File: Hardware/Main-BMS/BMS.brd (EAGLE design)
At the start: 114.3 x 124.5 mm, 99 parts, among them IC1 ACS759, IC2 SMI-1324-TW-5V-2-R, Q1 2N7002PW, Q10 2N7002PW, Q2 2N7002PW, Q5 2N7002PW, Q6 2N7002PW, Q7 2N7002PW, Q8 2N7002PW, Q9 2N7002PW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

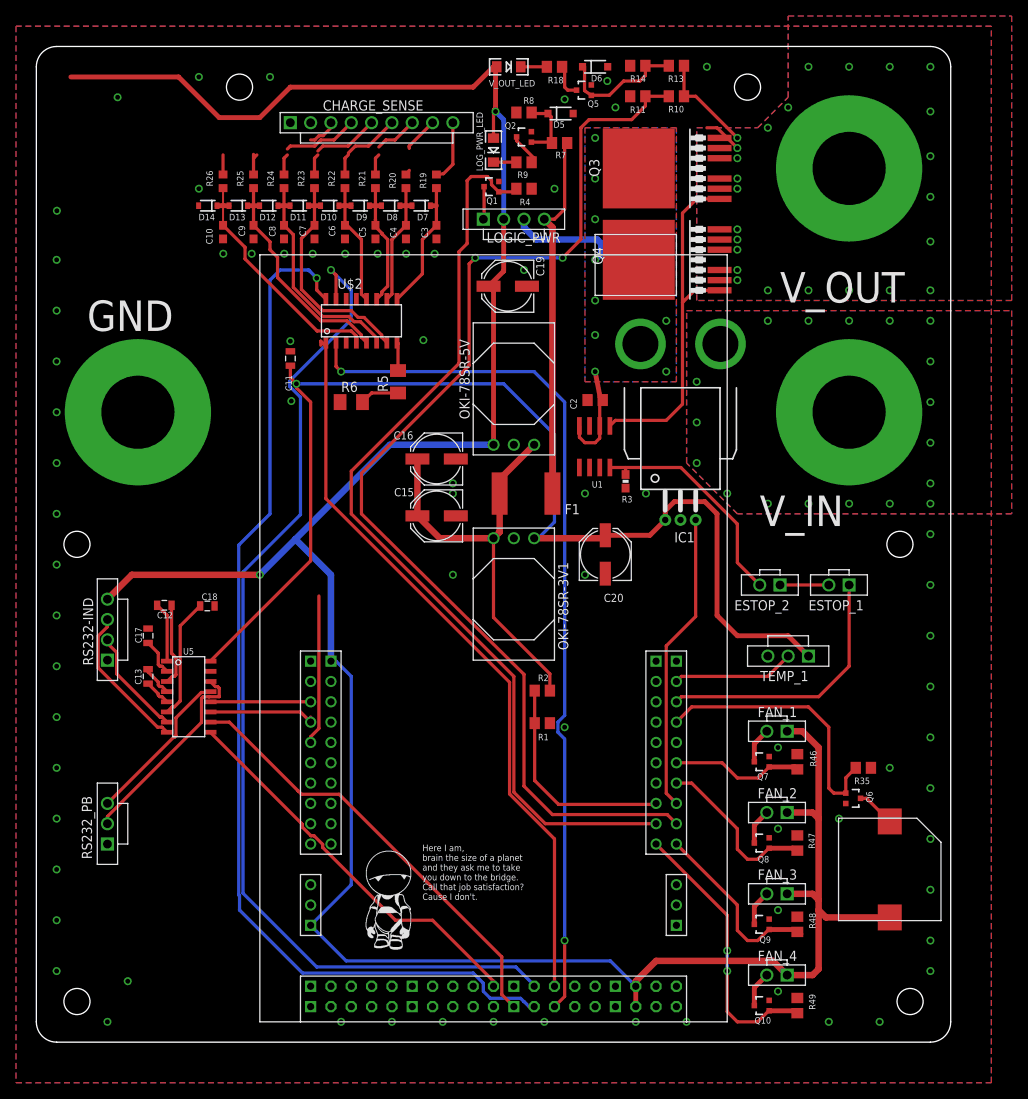
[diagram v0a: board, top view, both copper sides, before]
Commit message: Fixed connector placement, switched to 3v3 UART for indicator board and added protection zeners, replaced ACS759 with ACS770.
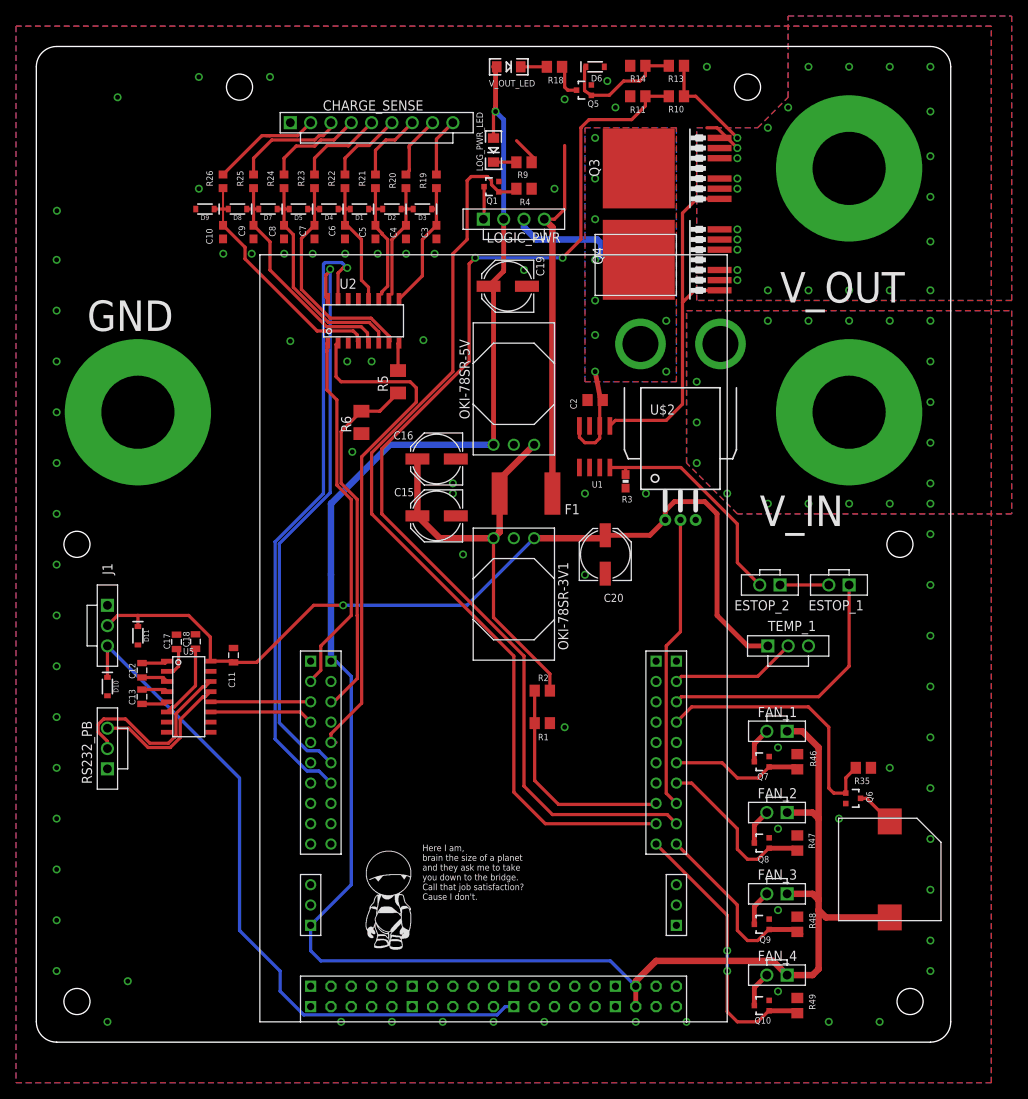
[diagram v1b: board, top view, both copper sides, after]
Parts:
- removed D12, D13, D14: PDZ7.5B, SparkFun-DiscreteSemi:SOD-323
- removed IC1: ACS759, MRDT-ICs:ACS-PFF-LEADFORM
- removed Q2: 2N7002PW, SparkFun-DiscreteSemi:SOT323
- removed R7: 1MΩ, rcl:R0805
- removed R8: 100kΩ, rcl:R0805
- removed RS232-IND: SL04VERT, MRDT-Connectors:MOLEX-70543-0003
- added D1, D2, D3, D4: 7.5V, SparkFun-DiscreteSemi:SOD-323
- added J1: SL03, MRDT-Connectors:MOLEX-70543-0002
- added U2: MUX508, MRDT-ICs:SOIC16
- D10, D11: value PDZ7.5B -> 3.6V
- D5: value BZT52C15-7-F -> 7.5V; device SparkFun-DiscreteSemi:SOD-123 -> SparkFun-DiscreteSemi:SOD-323
- D6: value BZT52C15-7-F -> 3.6V; device SparkFun-DiscreteSemi:SOD-123 -> SparkFun-DiscreteSemi:SOD-323
- D7, D8, D9: value PDZ7.5B -> 7.5V
- U$2: value MUX508 -> ACS770; device MRDT-ICs:SOIC16 -> MRDT-ICs:ACS-PFF-LEADFORM
- moved D10 66.2 mm to (8.89, 44.5), turned to 270 degrees
- moved D11 57.4 mm to (12.7, 50.8), turned to 270 degrees
- moved U$2 47.0 mm to (80.5, 65.3)
- moved C11 37.8 mm to (24.6, 48.4)
- moved D5 34.9 mm to (32.8, 104.1), turned to 180 degrees
- moved D9 19.4 mm to (21.1, 104.1)
- moved D7 19.2 mm to (29.0, 104.1)
- moved D8 19.2 mm to (25.1, 104.1)
- moved RS232_PB 9.40 mm to (8.89, 36.7)
- moved C12 8.59 mm to (13.2, 46.5), turned to 270 degrees
- moved C18 4.69 mm to (19.9, 50.1), turned to 90 degrees
- moved C17 3.64 mm to (17.5, 50.0)
- moved R6 2.84 mm to (40.6, 77.5), turned to 90 degrees
- moved C13 2.65 mm to (13.2, 43.2)
- moved TEMP_1 1.27 mm to (94.0, 49.5), turned to 180 degrees
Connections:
- removed net GAUGE_ON: U3.9.0
- removed net LED_CLR: U3.9.1
- removed net LED_SRCK: U3.8.7
- removed net N$13: D5.C, Q2.1, R7.2, R8.1
- removed net N$23: U$2.13
- removed net N$5: IC1.P$2, V_IN.P$1
- removed net RS232_RX_IND: RS232-IND.3, U5.8
- removed net RS232_TX_IND: RS232-IND.2, U5.7
- net +3V3: now also D11.C, J1.2, U$2.1; no longer IC1.1
- net 5V: no longer RS232-IND.4
- net ADC_CELL_A0: now also U2.1, U3.6.0; no longer U$2.1, U3.7.6
- net ADC_CELL_A1: now also U2.16, U3.4.4; no longer U$2.16, U3.7.5
- net ADC_CELL_A2: now also U2.15, U3.4.5; no longer U$2.15, U3.7.4
- net ADC_CELL_EN: now also U2.2, U3.4.2; no longer U$2.2, U3.7.7
- net ADC_CELL_VOUT: now also U3.6.1; no longer U3.4.1
- net CELL_1_FILTER: now also D8.A, D9.C, U2.4; no longer D13.A, D14.C, U$2.4
- net CELL_2_FILTER: now also D7.A, D8.C, U2.5; no longer D12.A, D13.C, U$2.5
- net CELL_3_FILTER: now also D5.A, D7.C, U2.6; no longer D11.A, D12.C, U$2.6
- net CELL_4_FILTER: now also D4.A, D5.C, U2.7; no longer D10.A, D11.C, U$2.7
- net CELL_5_FILTER: now also D1.A, D4.C, U2.12; no longer D10.C, D9.A, U$2.12
- net CELL_6_FILTER: now also D1.C, D2.A, U2.11; no longer D8.A, D9.C, U$2.11
- net CELL_7_FILTER: now also D2.C, D3.A, U2.10; no longer D7.A, D8.C, U$2.10
- net CELL_8_FILTER: now also D3.C, U2.9; no longer D7.C, U$2.9
- net GND: now also D10.A, D11.A, D9.A, J1.1, R9.2, U2.3; no longer D14.A, D5.A, IC1.2, Q2.2, R8.2, RS232-IND.1, U$2.14
- net N$11: now also U$2.P$2, V_IN.P$1; no longer Q2.3, R9.2
- net N$15: no longer R7.1
- net N$22: now also U2.8; no longer U$2.8
- net N$41: now also U$2.P$1; no longer IC1.P$1
- net PACK_I_MEAS: now also U$2.2; no longer IC1.3
- net SER_RX_IND: no longer U5.9
- net SER_TX_IND: now also D10.C, J1.3; no longer U5.10
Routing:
- net 5V: track 342.7 -> 258.0 mm, vias 2 -> 1
- net ADC_CELL_A1: track 132.9 -> 72.0 mm
- net ADC_CELL_A2: track 130.9 -> 79.1 mm
- net SER_RX_IND: track 49.4 -> 0.00 mm
- net ADC_CELL_A0: track 92.3 -> 45.9 mm
- net ADC_CELL_EN: track 110.2 -> 64.4 mm, vias 2 -> 0
- net +3V3: track 144.7 -> 112.6 mm
- net SER_TX_IND: track 55.5 -> 86.9 mm
- net ADC_CELL_VOUT: track 23.7 -> 45.3 mm
- net RS232_RX_IND: track 18.5 -> 0.00 mm
- net RS232_TX_IND: track 13.5 -> 0.00 mm
- net CELL_1: track 2.45 -> 14.1 mm
- net N$13: track 8.45 -> 0.00 mm
- net N$42: track 10.4 -> 3.35 mm
- net CELL_2: track 6.28 -> 13.3 mm
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- added copper zone on layer 1, net N$11
- removed copper zone on layer 1, net N$5

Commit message: Updated to actually match last commit
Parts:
- moved D10 15.0 mm to (9.14, 59.4), turned to 90 degrees
- turned J1 to 270 degrees
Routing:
- net SER_TX_IND: track 86.9 -> 91.8 mm
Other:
- board text added: "SER_IND"
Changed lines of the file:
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@@
 Call that job satisfaction?
 Cause I don't.</text>
+<text x="6.35" y="48.26" size="1.27" layer="21" rot="R90">SER_IND</text>
 </plain>
 <attributes>
@@
 <element name="R5" library="rcl" package="M1206" value="1M" x="45.212" y="82.55" rot="R90"/>
 <element name="R6" library="rcl" package="M1206" value="100k" x="40.64" y="77.47" rot="R90"/>
-<element name="J1" library="MRDT-Connectors" package="MOLEX-70543-0002" value="SL03" x="8.89" y="52.07" rot="R90"/>
+<element name="J1" library="MRDT-Connectors" package="MOLEX-70543-0002" value="SL03" x="8.89" y="52.07" rot="R270"/>
 <element name="U2" library="MRDT-ICs" package="SOIC16" value="MUX508" x="40.894" y="90.17"/>
 <element name="D1" library="SparkFun-DiscreteSemi" package="SOD-323" value="7.5V" x="40.386" y="104.14" rot="R180">
@@
 </element>
 <element name="U$2" library="MRDT-ICs" package="ACS-PFF-LEADFORM" value="ACS770" x="80.518" y="65.278"/>
-<element name="D10" library="SparkFun-DiscreteSemi" package="SOD-323" value="3.6V" x="8.89" y="44.45" rot="R270">
-<attribute name="PROD_ID" value="DIO-08199" x="8.89" y="44.45" size="1.778" layer="27" rot="R270" display="off"/>
+<element name="D10" library="SparkFun-DiscreteSemi" package="SOD-323" value="3.6V" x="9.144" y="59.436" rot="R90">
+<attribute name="PROD_ID" value="DIO-08199" x="9.144" y="59.436" size="1.778" layer="27" rot="R90" display="off"/>
 </element>
 <element name="D11" library="SparkFun-DiscreteSemi" package="SOD-323" value="3.6V" x="12.7" y="50.8" rot="R270">
@@
 <wire x1="24.6488" y1="47.4698" x2="27.53545625" y2="47.4698" width="0.4064" layer="1"/>
 <contactref element="J1" pad="2"/>
-<wire x1="10.16" y1="53.34" x2="8.89" y2="52.07" width="0.4064" layer="1"/>
-<wire x1="12.7" y1="53.34" x2="10.16" y2="53.34" width="0.4064" layer="1"/>
-<wire x1="12.7" y1="53.34" x2="19.05" y2="53.34" width="0.4064" layer="1"/>
+<wire x1="19.05" y1="53.34" x2="12.7" y2="53.34" width="0.4064" layer="1"/>
 <wire x1="19.05" y1="53.34" x2="21.75" y2="50.64" width="0.4064" layer="1"/>
 <wire x1="21.75" y1="50.64" x2="21.75" y2="47.625" width="0.4064" layer="1"/>
@@
 <wire x1="78.618" y1="65.278" x2="76.7" y2="63.36" width="0.6096" layer="1"/>
 <wire x1="12.7" y1="51.95" x2="12.7" y2="53.34" width="0.4064" layer="1"/>
+<wire x1="12.7" y1="53.34" x2="10.16" y2="53.34" width="0.4064" layer="1"/>
+<wire x1="10.16" y1="53.34" x2="8.89" y2="52.07" width="0.4064" layer="1"/>
 </signal>
 <signal name="N$3">
@@
 <contactref element="U3" pad="9.7"/>
 <contactref element="J1" pad="3"/>
-<wire x1="8.89" y1="49.53" x2="25.4" y2="33.02" width="0.4064" layer="16"/>
-<wire x1="25.4" y1="33.02" x2="25.4" y2="13.97" width="0.4064" layer="16"/>
 <wire x1="25.4" y1="13.97" x2="30.48" y2="8.89" width="0.4064" layer="16"/>
 <wire x1="30.48" y1="8.89" x2="30.48" y2="6.35" width="0.4064" layer="16"/>
@@
 <wire x1="33.4192" y1="3.4108" x2="57.57838125" y2="3.4108" width="0.4064" layer="16"/>
 <contactref element="D10" pad="C"/>
-<wire x1="8.89" y1="45.6" x2="8.89" y2="49.53" width="0.4064" layer="1"/>
+<wire x1="8.89" y1="54.61" x2="25.4" y2="38.1" width="0.4064" layer="16"/>
+<wire x1="25.4" y1="38.1" x2="25.4" y2="13.97" width="0.4064" layer="16"/>
+<wire x1="9.144" y1="58.286" x2="8.89" y2="58.032" width="0.4064" layer="1"/>
+<wire x1="8.89" y1="58.032" x2="8.89" y2="54.61" width="0.4064" layer="1"/>
 </signal>
 <signal name="SER_RX_PB">

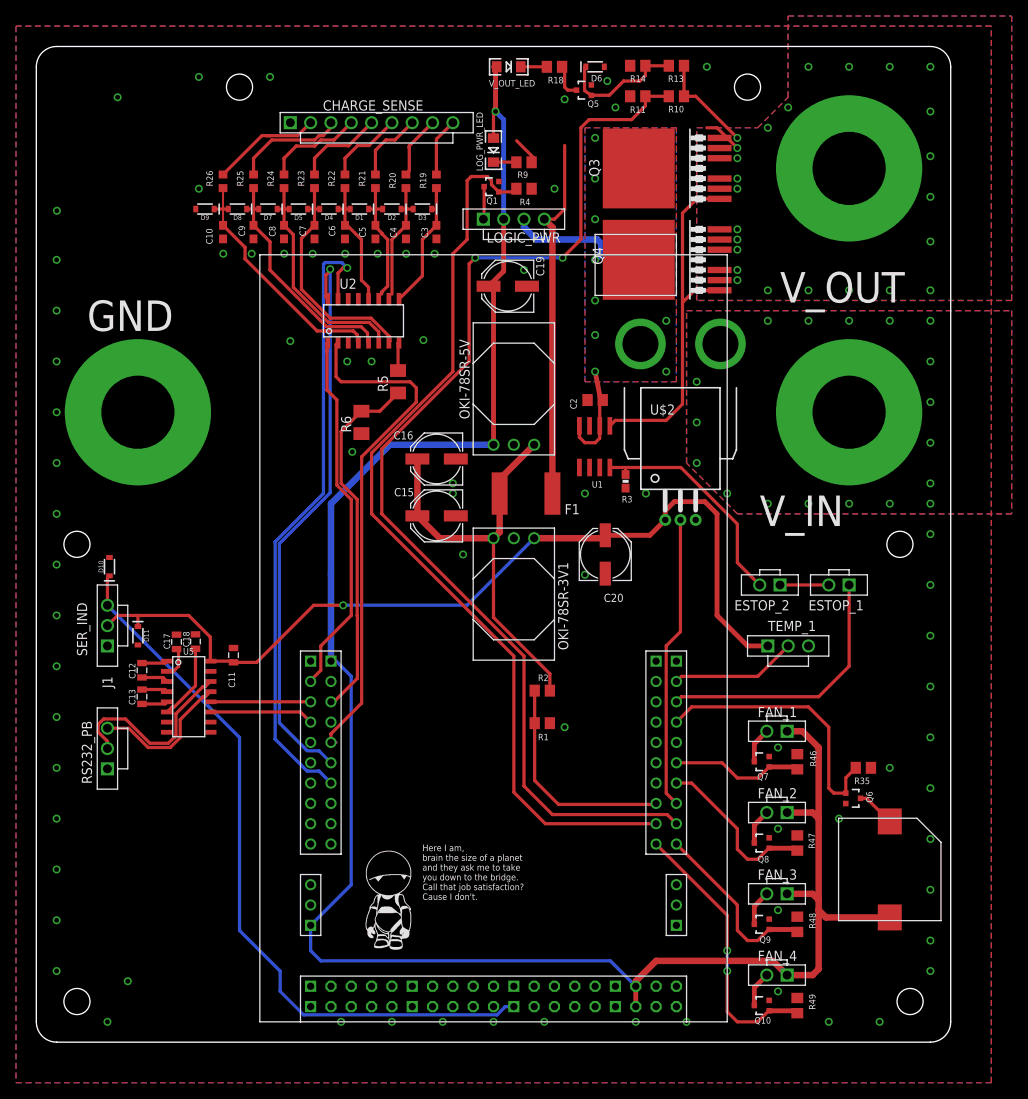
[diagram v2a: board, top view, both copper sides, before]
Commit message: Cleaned Routing and Silkscreen
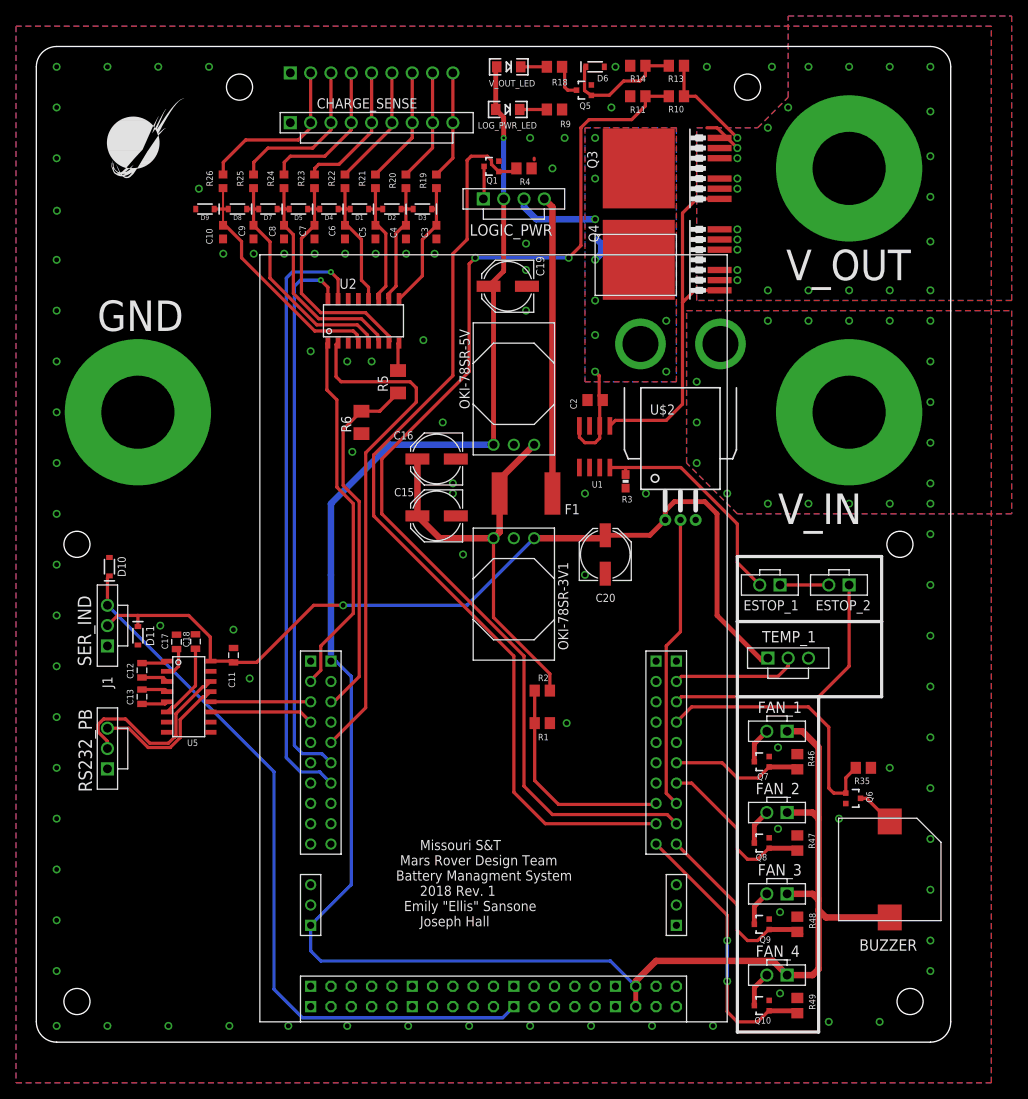
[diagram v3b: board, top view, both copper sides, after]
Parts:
- removed U$1: (no value), sig:MARVIN-THE-PARANOID-ANDROID
- removed U$17: (no value), sig:SANSONE-SIG
- added CHARGE_SENSE1: SL09, MRDT-Connectors:MOLEX-70543-0008
- moved U$9 19.3 mm to (8.81, 107.2), flipped to the top
- moved R9 7.62 mm to (64.8, 116.6)
- moved LOG_PWR_LED 5.38 mm to (58.9, 116.6), turned to 0 degrees
- moved Q1 2.54 mm to (56.9, 109.5)
- moved LOGIC_PWR 2.54 mm to (59.7, 105.4)
- moved R4 2.54 mm to (61.0, 109.2)
- moved TEMP_1 1.52 mm to (94.0, 48.0)
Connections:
- net CELL_1: now also CHARGE_SENSE1.2
- net CELL_2: now also CHARGE_SENSE1.3
- net CELL_3: now also CHARGE_SENSE1.4
- net CELL_4: now also CHARGE_SENSE1.5
- net CELL_5: now also CHARGE_SENSE1.6
- net CELL_6: now also CHARGE_SENSE1.7
- net CELL_7: now also CHARGE_SENSE1.8
- net CELL_8: now also CHARGE_SENSE1.9
- net GND: now also CHARGE_SENSE1.1
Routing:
- net N$15: track 45.7 -> 37.3 mm
- net CELL_2: track 13.3 -> 20.6 mm
- net CELL_1: track 14.1 -> 21.1 mm
- net CELL_3: track 12.3 -> 18.7 mm
- net CELL_8: track 7.33 -> 13.6 mm
- net CELL_4: track 11.1 -> 17.1 mm
- net CELL_7: track 8.10 -> 14.1 mm
- net CELL_6: track 9.05 -> 14.6 mm
- net CELL_5: track 9.74 -> 15.1 mm
- net 5V: track 258.0 -> 253.7 mm
- net GND: track 3.74 -> 0.19 mm, vias 73 -> 87
- net ADC_CELL_A1: track 72.0 -> 69.2 mm
- net ADC_CELL_A2: track 79.1 -> 76.5 mm
- net LOGIC_SWITCH: track 115.8 -> 118.1 mm
- net CELL_7_FILTER: track 15.4 -> 16.6 mm
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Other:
- board text added: "BUZZER"
- board text added: "Missouri S&T Mars Rover Design Team Battery Managment System 2018 Rev. 1 Emily "Ellis" Sansone Joseph Hall"
- board text removed: "Here I am, brain the size of a planet and they ask me to take you down to the bridge. Call that job satisfaction? Cause I don't."
- board text removed: "Missouri S&T Mars Rover Design Team Battery Management System Rev. 2, Gryphon Emily "Ellis" Sansone"

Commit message: Cleaned up fonts, connectors, MUX508 traces and symbol. Removed some via stitching to reduce short potential with drill-hole washers.
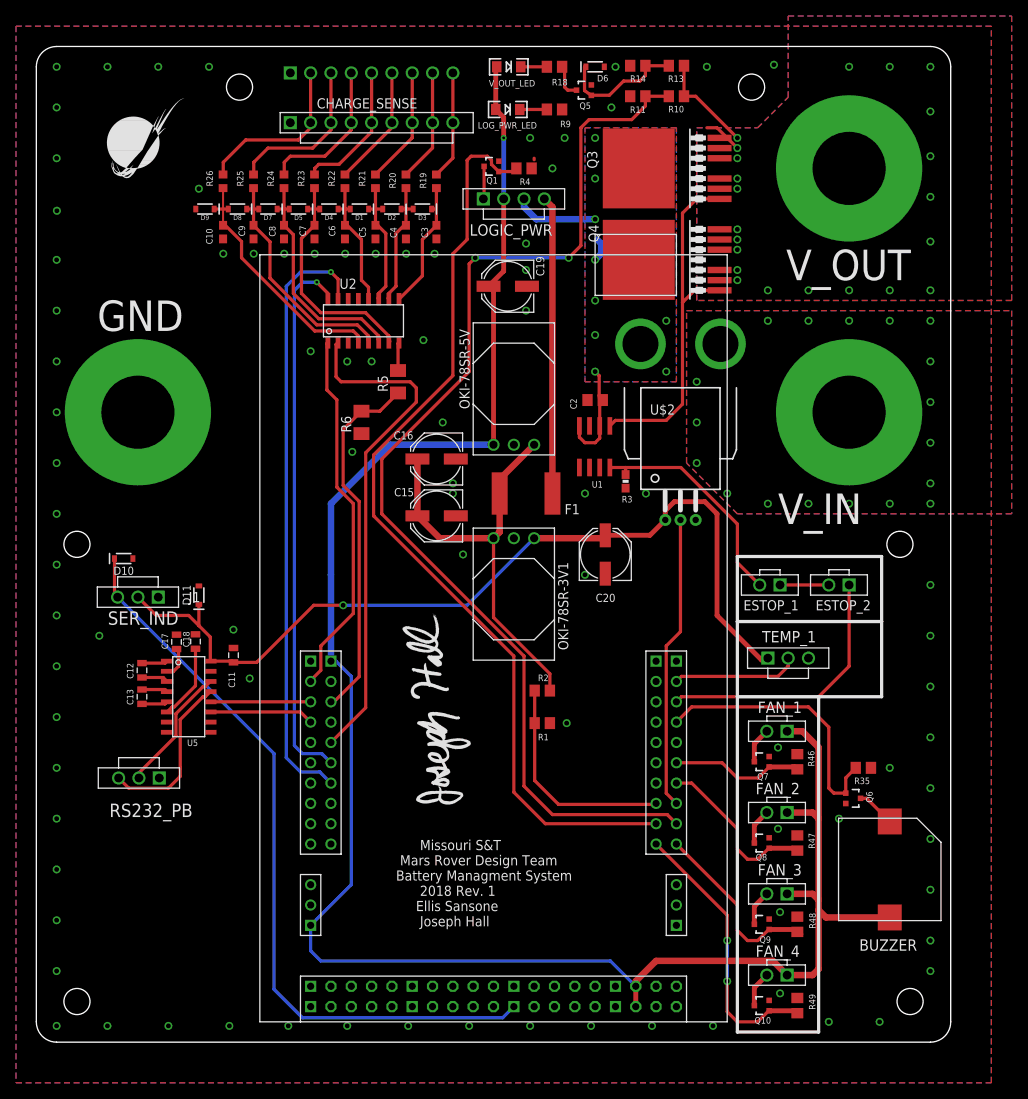
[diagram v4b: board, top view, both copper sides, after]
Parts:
- added U$1: (no value), MRDT-Signatures:JOSEPH_HALL_SIGNATURE
- moved D11 9.16 mm to (20.3, 55.9), turned to 90 degrees
- moved RS232_PB 5.39 mm to (12.8, 33.0), turned to 0 degrees
- moved J1 5.21 mm to (12.7, 55.6), turned to 0 degrees
- moved D10 2.05 mm to (10.9, 60.5), turned to 0 degrees
- moved H4 0.51 mm to (89.4, 119.4)
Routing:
- net RS232_TX_PB: track 23.9 -> 15.9 mm
- net RS232_RX_PB: track 18.1 -> 21.2 mm
- net +3V3: track 113.4 -> 111.3 mm
- net SER_TX_IND: track 92.4 -> 94.1 mm
- net ADC_CELL_A1: track 69.2 -> 68.3 mm
- net ADC_CELL_A2: track 76.5 -> 75.9 mm
- net N$3: vias 25 -> 22
- net GND: vias 87 -> 86
- added copper zone on layer 16, net N$11
- removed copper zone on layer 16, net N$5
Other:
- board text added: "Missouri S&T Mars Rover Design Team Battery Managment System 2018 Rev. 1 Ellis Sansone Joseph Hall"
- board text removed: "Missouri S&T Mars Rover Design Team Battery Managment System 2018 Rev. 1 Emily "Ellis" Sansone Joseph Hall"
